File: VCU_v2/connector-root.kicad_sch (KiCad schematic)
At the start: 12 parts, among them J4 Micro_SD_Card, U6 MX150 20-pin, U7 MX150 20-pin, U8 MX150 20-pin

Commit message: vcu v2 schematics done
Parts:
- removed R41: 120, Resistor_SMD:R_0603_1608Metric_Pad0.98x0.95mm_HandSolder, symbol BFR Resistors:RMCF0603FT120R
- removed U6, U7, U8: MX150 20-pin, 20pinMX150Header:CONN_SD-34829-001_20_ST_MOL, symbol Molex-MX150:MX150_20-pin_2x10_Board_Connector
- added R9: 120, Resistor_SMD:R_0603_1608Metric_Pad0.98x0.95mm_HandSolder, symbol BFR Resistors:RMCF0603FT120R
- added U5, U6, U7: ~, symbol Molex-MX150:MX150L_16-pin
- renumbered J4 to J2, TP45 to TP21, TP46 to TP22, TP44 to TP23, TP43 to TP24, TP47 to TP25, TP42 to TP26
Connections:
- net APPS1-4.8V: now also U5.6
- net APPS1-GND: now also U5.9
- net APPS1-SIG: now also U5.1
- net APPS2-4.8V: now also U5.5
- net APPS2-GND: now also U5.10
- net APPS2-SIG: now also U5.2
- net BMS-FAULT: now also U6.6
- net BMS_FAULT+: now also U7.8
- net BMS_FAULT-: now also U7.16
- net BRAKE_LIGHT: now also U7.5
- net BSE-4.8V: now also U5.4
- net BSE-GND: now also U5.11
- net BSE-SIG: now also U5.3
- net BSPD-FAULT: now also U6.4
- net BSPD_FAULT+: now also U7.6
- net BSPD_FAULT-: now also U7.14
- net CAN1_H: now also R9.1, U5.13
- net CAN1_L: now also U5.12
- net GEN_BTN1+: now also U7.1
- net GEN_BTN1-: now also U7.9
- net GEN_BTN2+: now also U7.2
- net GEN_BTN2-: now also U7.10
- net GPIO_10: now also U6.13
- net GPIO_11: now also U6.12
- net GPIO_13: now also U6.11
- net GPIO_14: now also U6.10
- net GPIO_19: now also U6.15
- net GPIO_20: now also U6.16
- net GPIO_5: now also U7.3
- net GPIO_6: now also U7.4
- net GPIO_9: now also U6.14
- net GPIO_PWM_1: now also U7.13
- net GPIO_PWM_2: now also U7.12
- net GPIO_PWM_3: now also U7.11
- net GPIO_PWM_4: now also U5.14
- net IMD-FAULT: now also U6.5
- net IMD_FAULT+: now also U7.7
- net IMD_FAULT-: now also U7.15
- net PRECHARGE_BTN+: now also U5.15
- net PRECHARGE_BTN-: now also U5.16
- net RTD_BTN+: now also U5.8
- net RTD_BTN-: now also U5.7
- net SPEAKER+: now also U6.8
- net SPEAKER-: now also U6.7
- net Vin+: now also U6.1
- net Vin-: now also U6.9
- net at JP2.2 (C): now also R9.2
- new net Isense-active: U6.3
- new net Isense-thresh: U6.2
- no-connect marks 8 -> 1

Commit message: placements friggin 80% friggin done shoutout epstein
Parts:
- U17: renamed from U5; footprint (none) -> 20pinMX150Header:CONN_SD-19427-025_MOL
- U18: renamed from U6; footprint (none) -> 20pinMX150Header:CONN_SD-19427-025_MOL
- U19: renamed from U7; footprint (none) -> 20pinMX150Header:CONN_SD-19427-025_MOL
- renumbered J2 to J4, JP2 to JP4, R9 to R89, TP26 to TP42, TP24 to TP43, TP23 to TP44, TP21 to TP45, TP22 to TP46, TP25 to TP47
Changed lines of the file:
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@@
 		(dnp no)
 		(fields_autoplaced yes)
-		(property "Reference" "U6"
+		(property "Reference" "U18"
 			(at 166.37 46.9899 0)
 			(effects
@@
 				)
 				(justify right)
-				(hide yes)
 			)
 		)
@@
 			)
 		)
-		(property "Footprint" ""
+		(property "Footprint" "20pinMX150Header:CONN_SD-19427-025_MOL"
 			(at 162.56 48.26 0)
 			(effects
@@
 			(project "VCU_v2"
 				(path "/4ee6c2ad-9a1b-4276-b3cf-1cc8dc52967e/7728fa73-43ca-4882-a7da-9eb85b8c7f39"
-					(reference "U6")
+					(reference "U18")
 					(unit 1)
 				)
@@
 		(dnp no)
 		(fields_autoplaced yes)
-		(property "Reference" "J2"
+		(property "Reference" "J4"
 			(at 255.905 114.3 0)
 			(effects
@@
 			(project ""
 				(path "/4ee6c2ad-9a1b-4276-b3cf-1cc8dc52967e/7728fa73-43ca-4882-a7da-9eb85b8c7f39"
-					(reference "J2")
+					(reference "J4")
 					(unit 1)
 				)
@@
 		(on_board yes)
 		(dnp no)
-		(property "Reference" "TP22"
+		(property "Reference" "TP46"
 			(at 190.2468 140.7937 0)
 			(effects
@@
 			(project "VCU_v1"
 				(path "/4ee6c2ad-9a1b-4276-b3cf-1cc8dc52967e/7728fa73-43ca-4882-a7da-9eb85b8c7f39"
-					(reference "TP22")
+					(reference "TP46")
 					(unit 1)
 				)
@@
 		(on_board yes)
 		(dnp no)
-		(property "Reference" "R9"
+		(property "Reference" "R89"
 			(at 146.304 92.964 90)
 			(effects
@@
 			(project "VCU_v2"
 				(path "/4ee6c2ad-9a1b-4276-b3cf-1cc8dc52967e/7728fa73-43ca-4882-a7da-9eb85b8c7f39"
-					(reference "R9")
+					(reference "R89")
 					(unit 1)
 				)
@@
 		(on_board yes)
 		(dnp no)
-		(property "Reference" "TP25"
+		(property "Reference" "TP47"
 			(at 218.1868 144.6037 0)
 			(effects
@@
 			(project "VCU_v1"
 				(path "/4ee6c2ad-9a1b-4276-b3cf-1cc8dc52967e/7728fa73-43ca-4882-a7da-9eb85b8c7f39"
-					(reference "TP25")
+					(reference "TP47")
 					(unit 1)
 				)
@@
 		(dnp no)
 		(fields_autoplaced yes)
-		(property "Reference" "#PWR041"
+		(property "Reference" "#PWR061"
 			(at 189.23 128.27 0)
 			(effects
@@
 			(project ""
 				(path "/4ee6c2ad-9a1b-4276-b3cf-1cc8dc52967e/7728fa73-43ca-4882-a7da-9eb85b8c7f39"
-					(reference "#PWR041")
+					(reference "#PWR061")
 					(unit 1)
 				)
@@
 		(dnp no)
 		(fields_autoplaced yes)
-		(property "Reference" "#PWR043"
+		(property "Reference" "#PWR063"
 			(at 276.86 160.02 0)
 			(effects
@@
 			(project ""
 				(path "/4ee6c2ad-9a1b-4276-b3cf-1cc8dc52967e/7728fa73-43ca-4882-a7da-9eb85b8c7f39"
-					(reference "#PWR043")
+					(reference "#PWR063")
 					(unit 1)
 				)
@@
 		(dnp no)
 		(fields_autoplaced yes)
-		(property "Reference" "#PWR042"
+		(property "Reference" "#PWR062"
 			(at 204.47 144.78 0)
 			(effects
@@
 			(project ""
 				(path "/4ee6c2ad-9a1b-4276-b3cf-1cc8dc52967e/7728fa73-43ca-4882-a7da-9eb85b8c7f39"
-					(reference "#PWR042")
+					(reference "#PWR062")
 					(unit 1)
 				)
@@
 		(on_board yes)
 		(dnp no)
-		(property "Reference" "TP26"
+		(property "Reference" "TP42"
 			(at 228.3468 120.4737 0)
 			(effects
@@
 			(project "VCU_v1"
 				(path "/4ee6c2ad-9a1b-4276-b3cf-1cc8dc52967e/7728fa73-43ca-4882-a7da-9eb85b8c7f39"
-					(reference "TP26")
+					(reference "TP42")
 					(unit 1)
 				)
@@
 		(dnp no)
 		(fields_autoplaced yes)
-		(property "Reference" "JP2"
+		(property "Reference" "JP4"
 			(at 130.81 88.9001 90)
 			(effects
@@
 			(project "VCU_v2"
 				(path "/4ee6c2ad-9a1b-4276-b3cf-1cc8dc52967e/7728fa73-43ca-4882-a7da-9eb85b8c7f39"
-					(reference "JP2")
+					(reference "JP4")
 					(unit 1)
 				)
@@
 		(dnp no)
 		(fields_autoplaced yes)
-		(property "Reference" "U7"
+		(property "Reference" "U19"
 			(at 231.14 46.9899 0)
 			(effects
@@
 			)
 		)
-		(property "Footprint" ""
+		(property "Footprint" "20pinMX150Header:CONN_SD-19427-025_MOL"
 			(at 227.33 48.26 0)
 			(effects
@@
 			(project "VCU_v2"
 				(path "/4ee6c2ad-9a1b-4276-b3cf-1cc8dc52967e/7728fa73-43ca-4882-a7da-9eb85b8c7f39"
-					(reference "U7")
+					(reference "U19")
 					(unit 1)
 				)
@@
 		(on_board yes)
 		(dnp no)
-		(property "Reference" "TP21"
+		(property "Reference" "TP45"
 			(at 182.6268 130.6337 0)
 			(effects
@@
 			(project "VCU_v1"
 				(path "/4ee6c2ad-9a1b-4276-b3cf-1cc8dc52967e/7728fa73-43ca-4882-a7da-9eb85b8c7f39"
-					(reference "TP21")
+					(reference "TP45")
 					(unit 1)
 				)
@@
 		(on_board yes)
 		(dnp no)
-		(property "Reference" "TP24"
+		(property "Reference" "TP43"
 			(at 215.6468 123.0137 0)
 			(effects
@@
 			(project "VCU_v1"
 				(path "/4ee6c2ad-9a1b-4276-b3cf-1cc8dc52967e/7728fa73-43ca-4882-a7da-9eb85b8c7f39"
-					(reference "TP24")
+					(reference "TP43")
 					(unit 1)
 				)
@@
 	)
 	(symbol
+		(lib_name "MX150L_16-pin_1")
 		(lib_id "Molex-MX150:MX150L_16-pin")
 		(at 120.65 48.26 0)
@@
 		(dnp no)
 		(fields_autoplaced yes)
-		(property "Reference" "U5"
+		(property "Reference" "U17"
 			(at 124.46 46.9899 0)
 			(effects
@@
 			)
 		)
-		(property "Footprint" ""
+		(property "Footprint" "20pinMX150Header:CONN_SD-19427-025_MOL"
 			(at 120.65 48.26 0)
 			(effects
@@
 			(project ""
 				(path "/4ee6c2ad-9a1b-4276-b3cf-1cc8dc52967e/7728fa73-43ca-4882-a7da-9eb85b8c7f39"
-					(reference "U5")
+					(reference "U17")
 					(unit 1)
 				)
@@
 		(on_board yes)
 		(dnp no)
-		(property "Reference" "TP23"
+		(property "Reference" "TP44"
 			(at 201.6768 125.5537 0)
 			(effects
@@
 			(project "VCU_v1"
 				(path "/4ee6c2ad-9a1b-4276-b3cf-1cc8dc52967e/7728fa73-43ca-4882-a7da-9eb85b8c7f39"
-					(reference "TP23")
+					(reference "TP44")
 					(unit 1)
 				)

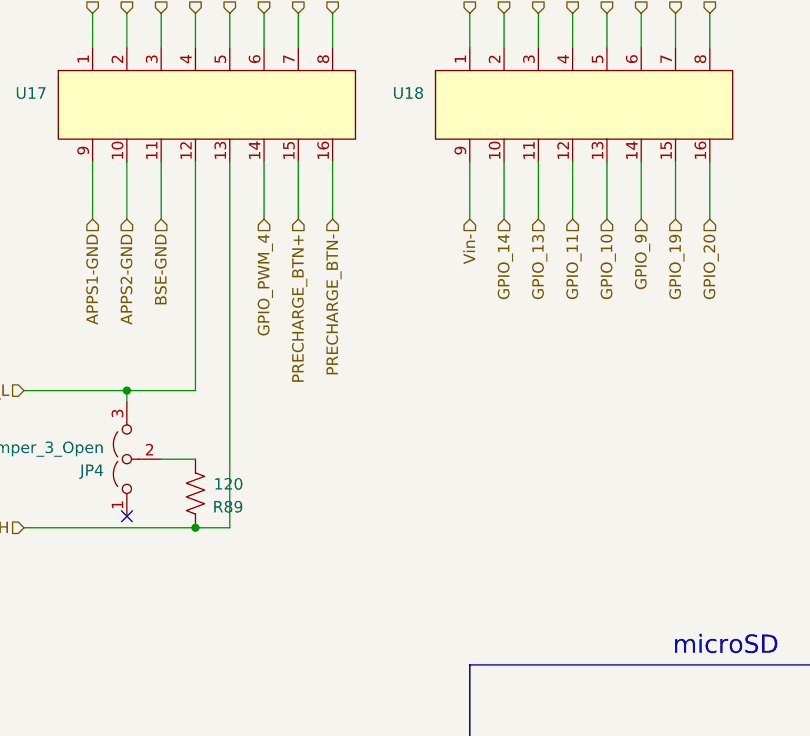
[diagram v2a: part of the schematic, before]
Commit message: slimed ethernet
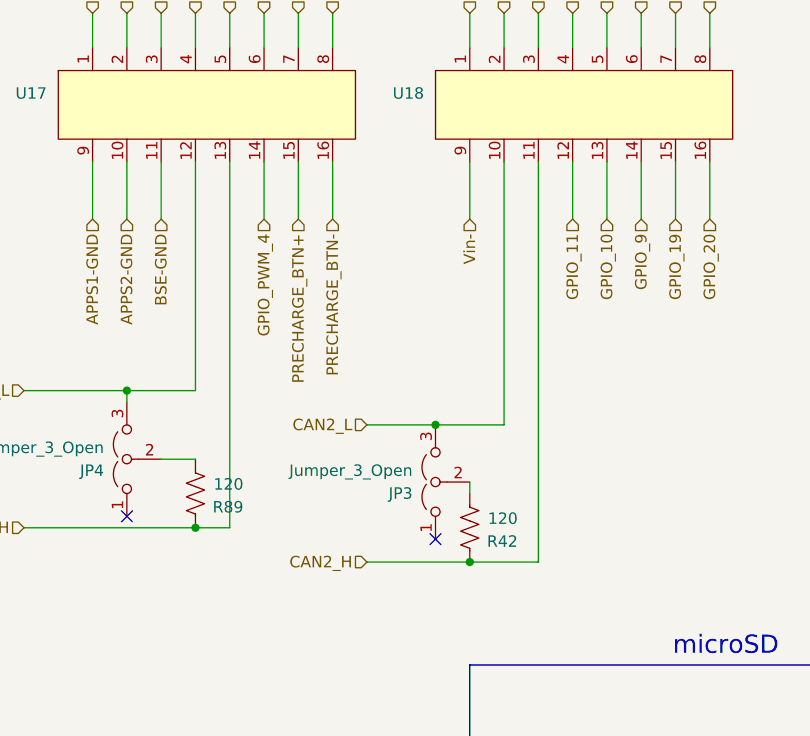
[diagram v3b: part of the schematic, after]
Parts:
- added JP3: Jumper_3_Open, Connector_PinHeader_2.54mm:PinHeader_1x03_P2.54mm_Vertical, symbol Jumper:Jumper_3_Open
- added R42: 120, Resistor_SMD:R_0603_1608Metric_Pad0.98x0.95mm_HandSolder, symbol BFR Resistors:RMCF0603FT120R
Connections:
- net GPIO_13 renamed CAN2_H
- net CAN2_H: now also R42.1
- net GPIO_14 renamed CAN2_L
- net CAN2_L: now also JP3.3 (B)
- new net: JP3.2 (C), R42.2
- no-connect marks 1 -> 2

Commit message: vcu v2 done
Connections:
- net CAN1_H: now also JP4.3 (B), U17.12; no longer R89.1, U17.13
- net CAN1_L: now also R89.1, U17.13; no longer JP4.3 (B), U17.12
- net GPIO_5: now also U18.1; no longer U19.3
- net GPIO_PWM_3: now also U18.9; no longer U19.11
- net Vin+: now also U19.3; no longer U18.1
- net Vin-: now also U19.11; no longer U18.9

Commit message: added silk to some shit
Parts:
- U17: Mouser P/N (none) -> 538-19427-0049; P/N (none) -> 194270049
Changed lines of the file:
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@@
 			)
 		)
-		(property "Datasheet" ""
+		(property "Datasheet" "https://www.molex.com/en-us/products/part-detail/194270049?display=pdf"
 			(at 120.65 48.26 0)
 			(effects
@@
 			(at 120.65 48.26 0)
 			(effects
+				(font
+					(size 1.27 1.27)
+				)
+				(hide yes)
+			)
+		)
+		(property "P/N" "194270049"
+			(at 120.65 48.26 0)
+			(effects
+				(font
+					(size 1.27 1.27)
+				)
+				(hide yes)
+			)
+		)
+		(property "Mouser P/N" "538-19427-0049 "
+			(at 120.65 48.26 0)
+			(effects

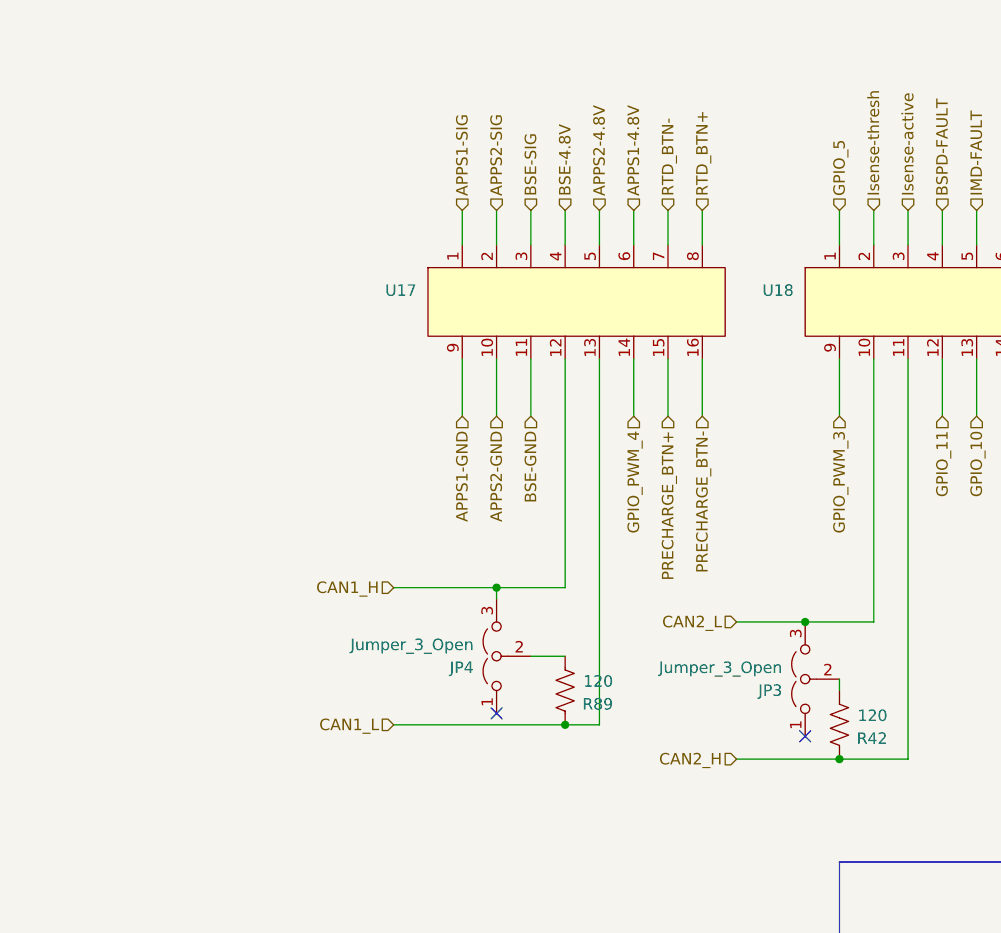
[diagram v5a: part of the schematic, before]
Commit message: Added connector for daq vcu
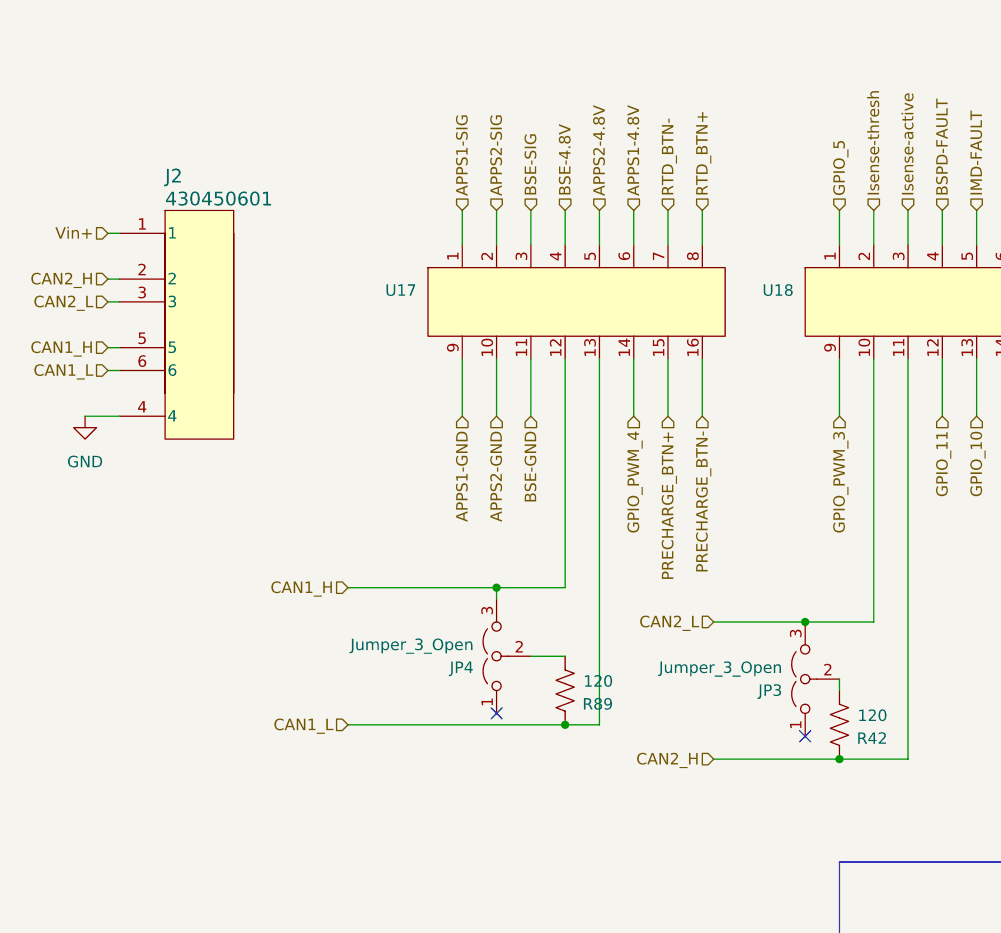
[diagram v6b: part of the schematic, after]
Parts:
- added J2: 430450601, 430450601:CONN_SD-43045-001_06_MOL, symbol 430450601:430450601
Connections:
- net CAN1_H: now also J2.5
- net CAN1_L: now also J2.6
- net CAN2_H: now also J2.2
- net CAN2_L: now also J2.3
- net GND: now also J2.4
- net Vin+: now also J2.1
